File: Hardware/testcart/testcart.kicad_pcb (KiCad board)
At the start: 2 copper layers, 53 x 37.5 mm, 15 parts, among them J10 Btn_A, J11 Btn_X, J12 Power, J13 Display, J14 Earth_Buttons, J15 Earth_Buzzer, J2 Buzzer, J3 Btn_Down, J4 Btn_Right, J5 Btn_B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

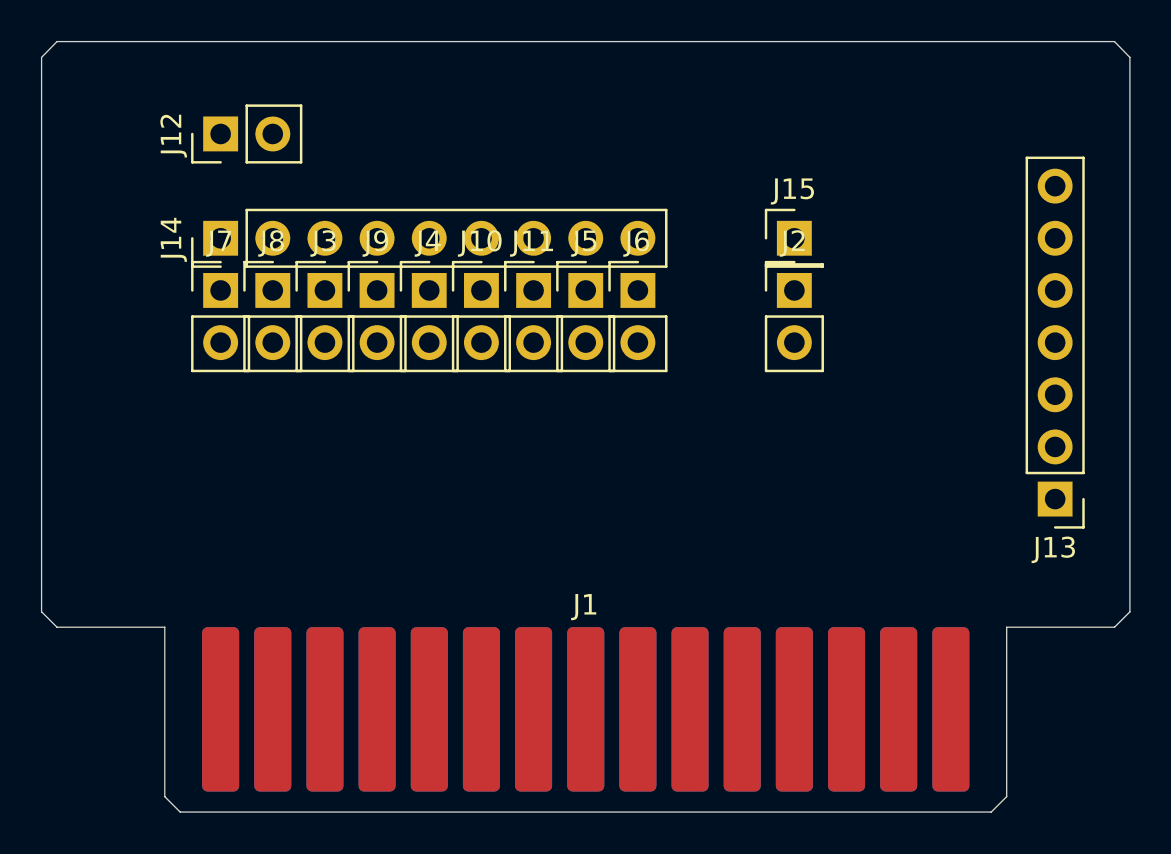
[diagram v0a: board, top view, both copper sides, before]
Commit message: Finish design of Test Cart
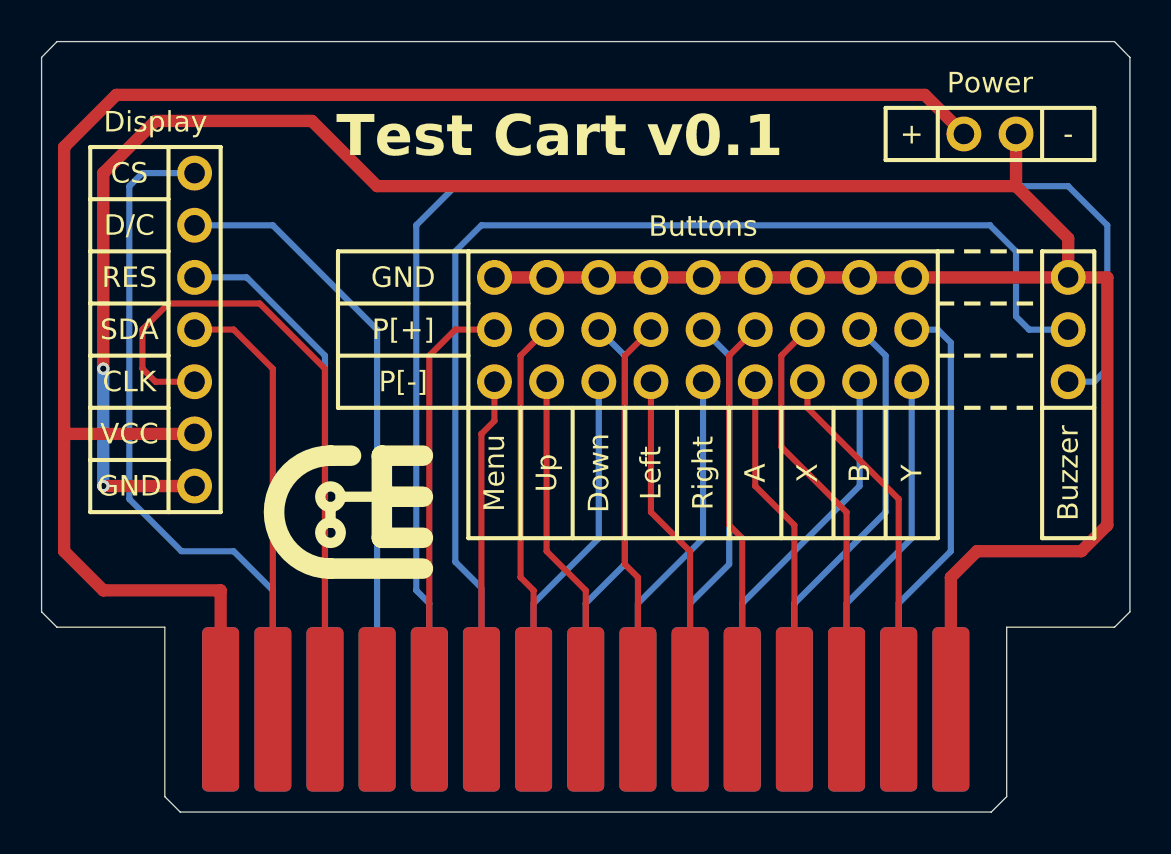
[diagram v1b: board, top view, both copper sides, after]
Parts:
- added REF**: Logo, carts:Logo, F.Cu at (128.3, 87.0)
- J10, J11, J12, J2, J3, J4, J5, J6, J7, J8, J9: footprint Connector_PinHeader_2.54mm:PinHeader_1x02_P2.54mm_Vertical -> carts:PinHeader_1x02_Abstract
- J13: footprint Connector_PinHeader_2.54mm:PinHeader_1x07_P2.54mm_Vertical -> carts:PinHeader_1x07_Abstract
- J14: footprint Connector_PinHeader_2.54mm:PinHeader_1x09_P2.54mm_Vertical -> carts:PinHeader_1x09_Abstract
- J15: footprint Connector_PinHeader_2.54mm:PinHeader_1x01_P2.54mm_Vertical -> carts:PinHeader_1x01_Abstract
- moved J13 44.8 mm to (120.7, 70.5), turned to 0 degrees
- moved J12 36.2 mm to (158.1, 68.6)
- moved J10 14.1 mm to (148.0, 80.6), turned to 180 degrees
- moved J11 14.1 mm to (150.5, 80.6), turned to 180 degrees
- moved J3 14.1 mm to (140.3, 80.6), turned to 180 degrees
- moved J5 14.1 mm to (153.0, 80.6), turned to 180 degrees
- moved J9 14.1 mm to (142.9, 80.6), turned to 180 degrees
- moved J7 14.1 mm to (135.3, 80.6), turned to 180 degrees
- moved J8 14.1 mm to (137.8, 80.6), turned to 180 degrees
- moved J2 14.1 mm to (163.2, 80.6), turned to 180 degrees
- moved J4 14.1 mm to (145.4, 80.6), turned to 180 degrees
- moved J6 14.1 mm to (155.6, 80.6), turned to 180 degrees
- moved J14 13.5 mm to (135.3, 75.6)
- moved J15 13.5 mm to (163.2, 75.6)
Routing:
- net GND: track 0.00 -> 131.6 mm, vias 0 -> 2
- net VCC: track 0.00 -> 85.9 mm
- net Net-(J1-BUZZ[+]): track 0.00 -> 68.2 mm
- net Net-(J1-BUZZ[-]): track 0.00 -> 57.2 mm
- net Net-(J1-SCR_CS): track 0.00 -> 33.3 mm
- net Net-(J1-SCR_SCL): track 0.00 -> 32.0 mm
- net Net-(J1-SCR_DC): track 0.00 -> 29.5 mm
- net Net-(J1-SCR_RES): track 0.00 -> 25.2 mm
- net Net-(J1-SCR_SDA): track 0.00 -> 21.2 mm
- net Net-(J1-BTN_Y2): track 0.00 -> 21.1 mm
- net Net-(J1-BTN_MENU1): track 0.00 -> 20.9 mm
- net Net-(J1-BTN_B2): track 0.00 -> 20.9 mm
- net Net-(J1-BTN_X1): track 0.00 -> 20.3 mm
- net Net-(J1-BTN_RIGHT2): track 0.00 -> 19.8 mm
- net Net-(J1-BTN_DOWN2): track 0.00 -> 19.8 mm
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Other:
- board text added: "+"
- board text added: "-"
- board text added: "A"
- board text added: "B"
- board text added: "Buttons"
- board text added: "Buzzer"
- board text added: "CLK"
- board text added: "CS"
- board text added: "D/C"
- board text added: "Display"
- board text added: "Down"
- board text added: "GND"
- board text added: "Left"
- board text added: "Menu"
- board text added: "P[+]"
- board text added: "P[-]"
- board text added: "Power"
- board text added: "RES"
- board text added: "Right"
- board text added: "SDA"
- board text added: "Test Cart v0.1"
- board text added: "Up"
- board text added: "VCC"
- board text added: "X"
- board text added: "Y"

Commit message: Add holes, add space for cartrige case
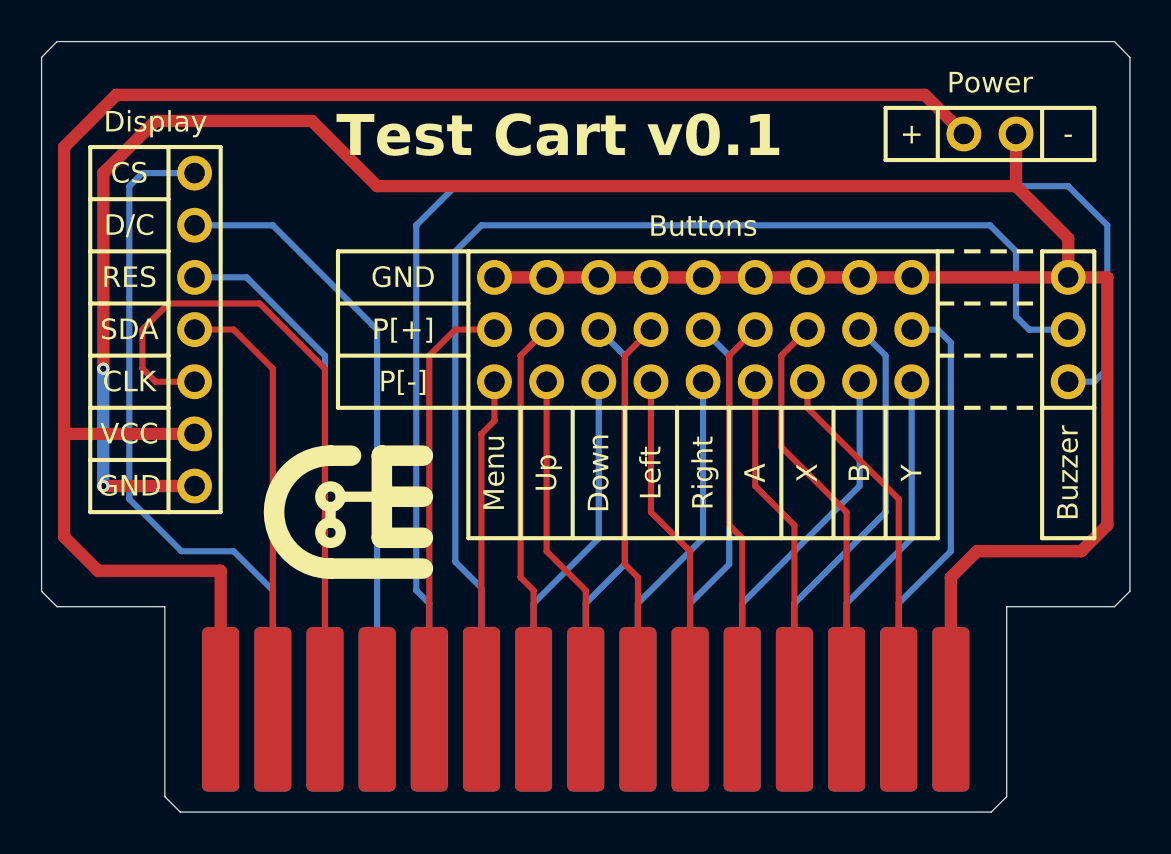
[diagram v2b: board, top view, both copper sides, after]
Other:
- outline, holes or cut-outs redrawn
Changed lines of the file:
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@@
 	)
 	(gr_line
-		(start 113.95 92.6)
-		(end 113.2 91.85)
+		(start 113.95 91.6)
+		(end 113.2 90.85)
 		(stroke
 			(width 0.05)
@@
 	)
 	(gr_line
-		(start 119.2 92.6)
+		(start 119.2 91.6)
 		(end 119.2 100.85)
 		(stroke
@@
 	)
 	(gr_line
-		(start 166.2 91.85)
+		(start 166.2 90.85)
 		(end 166.2 64.85)
 		(stroke
@@
 	)
 	(gr_line
-		(start 165.45 92.6)
-		(end 166.2 91.85)
+		(start 165.45 91.6)
+		(end 166.2 90.85)
 		(stroke
 			(width 0.05)
@@
 	)
 	(gr_line
-		(start 113.95 92.6)
-		(end 119.2 92.6)
+		(start 113.95 91.6)
+		(end 119.2 91.6)
 		(stroke
 			(width 0.05)
@@
 	)
 	(gr_line
-		(start 160.2 92.6)
-		(end 165.45 92.6)
+		(start 160.2 91.6)
+		(end 165.45 91.6)
 		(stroke
 			(width 0.05)
@@
 	(gr_line
 		(start 160.2 100.85)
-		(end 160.2 92.6)
+		(end 160.2 91.6)
 		(stroke
 			(width 0.05)
@@
 	(gr_line
 		(start 113.2 64.85)
-		(end 113.2 91.85)
+		(end 113.2 90.85)
 		(stroke
 			(width 0.05)
@@
 	)
 	(segment
-		(start 114.3 88.9)
-		(end 114.3 69.215)
+		(start 114.3 69.215)
+		(end 116.84 66.675)
 		(width 0.6)
 		(layer "F.Cu")
@@
 	)
 	(segment
+		(start 114.3 88.2)
+		(end 114.3 69.215)
+		(width 0.6)
+		(layer "F.Cu")
+		(net 15)
+	)
+	(segment
 		(start 121.92 96.6)
-		(end 121.92 90.805)
+		(end 121.92 89.85)
 		(width 0.6)
 		(layer "F.Cu")
@@
 	)
 	(segment
-		(start 116.205 90.805)
-		(end 114.3 88.9)
+		(start 115.95 89.85)
+		(end 114.3 88.2)
 		(width 0.6)
 		(layer "F.Cu")
@@
 	)
 	(segment
-		(start 114.3 69.215)
-		(end 116.84 66.675)
-		(width 0.6)
-		(layer "F.Cu")
-		(net 15)
-	)
-	(segment
-		(start 121.92 90.805)
-		(end 116.205 90.805)
-		(width 0.6)
-		(layer "F.Cu")
+		(start 121.92 89.85)
+		(end 115.95 89.85)
+		(width 0.6)
+		(layer "F.Cu")
